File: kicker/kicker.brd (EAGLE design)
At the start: 59.7 x 56.3 mm, 27 parts, among them T1 NPN_BC817,215, T2 NPN_BC817,215, T3 NPN_BC817,215, T4 NPN_BC817,215, X1 JST-XH-06-PIN-LONG-PAD

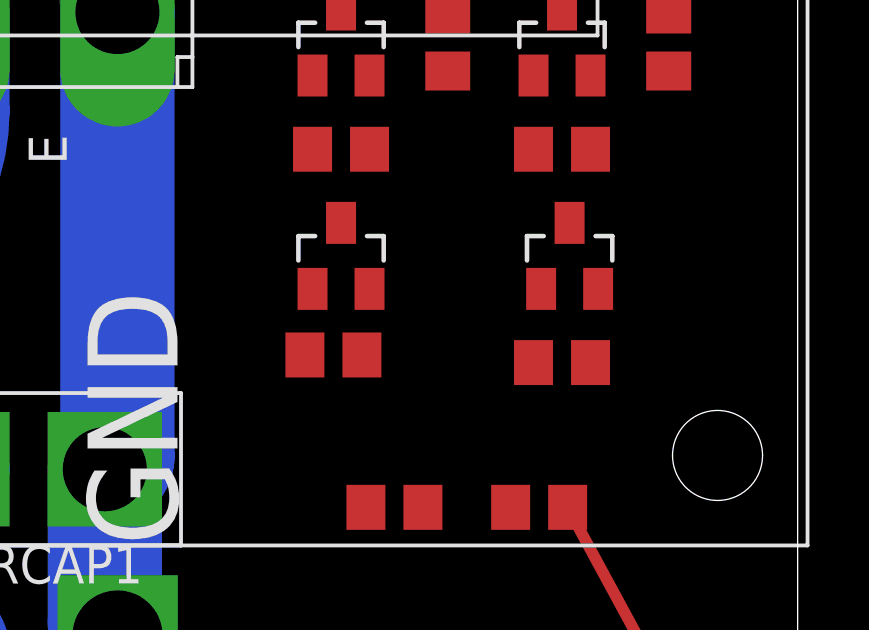
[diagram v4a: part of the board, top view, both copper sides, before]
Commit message: Adding optocoupler on the kick line
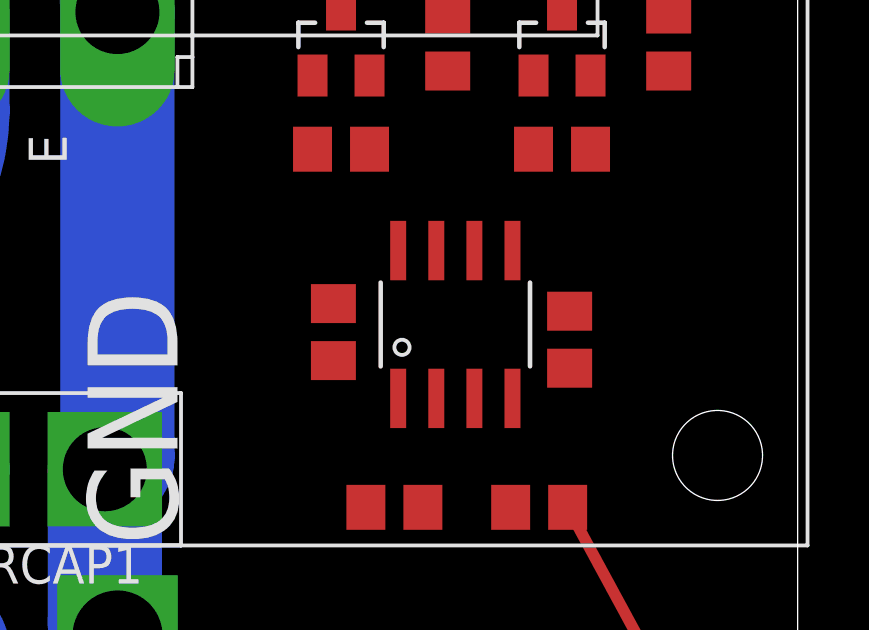
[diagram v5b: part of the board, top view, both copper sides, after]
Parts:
- removed R1, R4: 3K, rhoban:R0805
- removed T2, T4: NPN_BC817,215, rhoban:SOT-23
- added R7, R8: 3K, rhoban:R0805
- added U$4: ACPL-227-500E, rhoban:SO8
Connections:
- removed net N$1: R2.1, T1.1, T2.3
- removed net N$3: R32.1, T3.1, T4.3
- removed net N$5: R1.1, T2.1
- removed net N$6: R4.1, T4.1
- new net KICK_TR1: R2.1, T1.1
- new net KICK_TR2: R32.1, T3.1
- new net N$10: R8.1, U$4.3
- new net N$9: R7.1, U$4.1
- net GND: now also U$4.2, U$4.4; no longer T2.2, T4.2
- net KICK1: now also R7.2; no longer R1.2
- net KICK2: now also R8.2; no longer R4.2
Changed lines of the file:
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@@
 <element name="U$2" library="SparkFun-Hardware" package="STAND-OFF" value="" x="13.97" y="46.99"/>
 <element name="U$3" library="SparkFun-Hardware" package="STAND-OFF" value="" x="31.496" y="46.99"/>
-<element name="T2" library="rhoban" package="SOT-23" value="NPN_BC817,215" x="44.45" y="17.272">
-<attribute name="FARNELL" value="1081223" x="44.45" y="17.272" size="1.778" layer="27" display="off"/>
-</element>
-<element name="R1" library="rhoban" package="R0805" value="3K" x="44.196" y="13.97">
-<attribute name="FARNELL" value="2446965" x="44.196" y="13.97" size="1.778" layer="27" display="off"/>
-</element>
-<element name="T4" library="rhoban" package="SOT-23" value="NPN_BC817,215" x="52.07" y="17.272">
-<attribute name="FARNELL" value="1081223" x="52.07" y="17.272" size="1.778" layer="27" display="off"/>
-</element>
-<element name="R4" library="rhoban" package="R0805" value="3K" x="51.816" y="13.716">
-<attribute name="FARNELL" value="2446965" x="51.816" y="13.716" size="1.778" layer="27" display="off"/>
-</element>
 <element name="R5" library="rhoban" package="R0805" value="1K" x="44.45" y="28.702" rot="R270">
 <attribute name="FARNELL" value="2446965" x="44.45" y="28.702" size="1.778" layer="27" rot="R270" display="off"/>
@@
 <attribute name="FARNELL" value="2446965" x="51.816" y="28.702" size="1.778" layer="27" rot="R270" display="off"/>
 </element>
+<element name="U$4" library="rhoban" package="SO8" value="ACPL-227-500E" x="48.26" y="14.986" rot="R90">
+<attribute name="FARNELL" value="1634749RL" x="48.26" y="14.986" size="1.778" layer="27" rot="R90" display="off"/>
+</element>
+<element name="R7" library="rhoban" package="R0805" value="3K" x="44.196" y="14.732" rot="R90">
+<attribute name="FARNELL" value="2446965" x="44.196" y="14.732" size="1.778" layer="27" rot="R90" display="off"/>
+</element>
+<element name="R8" library="rhoban" package="R0805" value="3K" x="52.07" y="14.478" rot="R90">
+<attribute name="FARNELL" value="2446965" x="52.07" y="14.478" size="1.778" layer="27" rot="R90" display="off"/>
+</element>
 </elements>
 <signals>
 <signal name="KICK2">
 <contactref element="X1" pad="5"/>
-<contactref element="R4" pad="2"/>
-<wire x1="53.594" y1="1.27" x2="52.766" y2="13.716" width="0" layer="19" extent="1-1"/>
+<contactref element="R8" pad="2"/>
+<wire x1="52.07" y1="15.428" x2="53.594" y2="1.27" width="0" layer="19" extent="1-1"/>
 </signal>
 <signal name="GND" class="2">
@@
 <wire x1="25.654" y1="32.766" x2="29.63" y2="32.766" width="3.81" layer="16"/>
 <wire x1="29.63" y1="32.766" x2="36.996" y2="25.4" width="3.81" layer="16" curve="-90"/>
-<contactref element="T2" pad="2"/>
-<contactref element="T4" pad="2"/>
-<wire x1="53.02" y1="16.172" x2="52.766" y2="23.284" width="0" layer="19" extent="1-1"/>
+<contactref element="U$4" pad="2"/>
+<contactref element="U$4" pad="4"/>
 <wire x1="45.4" y1="23.284" x2="52.766" y2="23.284" width="0" layer="19" extent="1-1"/>
-<wire x1="45.4" y1="16.172" x2="45.4" y2="23.284" width="0" layer="19" extent="1-1"/>
-<wire x1="50.104" y1="8.89" x2="53.02" y2="16.172" width="0" layer="19" extent="1-1"/>
 <wire x1="36.996" y1="25.4" x2="45.4" y2="23.284" width="0" layer="19" extent="1-1"/>
 <wire x1="43.434" y1="1.27" x2="37" y2="0.17" width="0" layer="19" extent="16-16"/>
+<wire x1="50.104" y1="8.89" x2="43.434" y2="1.27" width="0" layer="19" extent="1-1"/>
 <wire x1="8.72" y1="14.92" x2="19.47" y2="25.4" width="0" layer="19" extent="1-1"/>
 <wire x1="11" y1="4.62" x2="8.72" y2="14.92" width="0" layer="19" extent="1-1"/>
+<wire x1="47.625" y1="12.5222" x2="11" y2="4.62" width="0" layer="19" extent="1-1"/>
+<wire x1="50.165" y1="12.5222" x2="47.625" y2="12.5222" width="0" layer="19" extent="1-1"/>
 </signal>
 <signal name="N$4">
@@
 <signal name="KICK1">
 <contactref element="X1" pad="4"/>
-<contactref element="R1" pad="2"/>
-<wire x1="51.054" y1="1.27" x2="45.146" y2="13.97" width="0" layer="19" extent="1-1"/>
+<contactref element="R7" pad="2"/>
+<wire x1="44.196" y1="15.682" x2="51.054" y2="1.27" width="0" layer="19" extent="1-1"/>
 </signal>
 <signal name="CAP">
@@
 <wire x1="6.52" y1="13.97" x2="3.81" y2="13.97" width="0.381" layer="1"/>
 </signal>
-<signal name="N$1">
+<signal name="KICK_TR1">
 <contactref element="R2" pad="1"/>
-<contactref element="T2" pad="3"/>
 <contactref element="T1" pad="1"/>
 <wire x1="43.5" y1="20.828" x2="43.5" y2="23.284" width="0" layer="19" extent="1-1"/>
-<wire x1="44.45" y1="18.372" x2="43.5" y2="20.828" width="0" layer="19" extent="1-1"/>
 </signal>
-<signal name="N$5">
-<contactref element="T2" pad="1"/>
-<contactref element="R1" pad="1"/>
-<wire x1="43.246" y1="13.97" x2="43.5" y2="16.172" width="0" layer="19" extent="1-1"/>
-</signal>
-<signal name="N$6">
-<contactref element="T4" pad="1"/>
-<contactref element="R4" pad="1"/>
-<wire x1="50.866" y1="13.716" x2="51.12" y2="16.172" width="0" layer="19" extent="1-1"/>
-</signal>
-<signal name="N$3">
-<contactref element="T4" pad="3"/>
+<signal name="KICK_TR2">
 <contactref element="R32" pad="1"/>
 <contactref element="T3" pad="1"/>
 <wire x1="50.866" y1="20.828" x2="50.866" y2="23.284" width="0" layer="19" extent="1-1"/>
-<wire x1="52.07" y1="18.372" x2="50.866" y2="20.828" width="0" layer="19" extent="1-1"/>
 </signal>
 <signal name="N$7">
@@
 <wire x1="8.47" y1="25.4" x2="51.816" y2="29.652" width="0" layer="19" extent="1-1"/>
 </signal>
+<signal name="N$9">
+<contactref element="U$4" pad="1"/>
+<contactref element="R7" pad="1"/>
+<wire x1="46.355" y1="12.5222" x2="44.196" y2="13.782" width="0" layer="19" extent="1-1"/>
+</signal>
+<signal name="N$10">
+<contactref element="U$4" pad="3"/>
+<contactref element="R8" pad="1"/>
+<wire x1="48.895" y1="12.5222" x2="52.07" y2="13.528" width="0" layer="19" extent="1-1"/>
+</signal>
 </signals>

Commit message: Fix optocoupler
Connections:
- net GND: now also U$4.5, U$4.7
- net KICK_TR1: now also U$4.8
- net KICK_TR2: now also U$4.6
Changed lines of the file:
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@@
 <contactref element="U$4" pad="2"/>
 <contactref element="U$4" pad="4"/>
-<wire x1="45.4" y1="23.284" x2="52.766" y2="23.284" width="0" layer="19" extent="1-1"/>
+<contactref element="U$4" pad="7"/>
+<contactref element="U$4" pad="5"/>
+<wire x1="50.165" y1="17.4498" x2="52.766" y2="23.284" width="0" layer="19" extent="1-1"/>
+<wire x1="47.625" y1="17.4498" x2="50.165" y2="17.4498" width="0" layer="19" extent="1-1"/>
+<wire x1="50.165" y1="12.5222" x2="50.165" y2="17.4498" width="0" layer="19" extent="1-1"/>
+<wire x1="47.625" y1="12.5222" x2="50.165" y2="12.5222" width="0" layer="19" extent="1-1"/>
+<wire x1="50.104" y1="8.89" x2="50.165" y2="12.5222" width="0" layer="19" extent="1-1"/>
+<wire x1="45.4" y1="23.284" x2="47.625" y2="17.4498" width="0" layer="19" extent="1-1"/>
 <wire x1="36.996" y1="25.4" x2="45.4" y2="23.284" width="0" layer="19" extent="1-1"/>
 <wire x1="43.434" y1="1.27" x2="37" y2="0.17" width="0" layer="19" extent="16-16"/>
-<wire x1="50.104" y1="8.89" x2="43.434" y2="1.27" width="0" layer="19" extent="1-1"/>
 <wire x1="8.72" y1="14.92" x2="19.47" y2="25.4" width="0" layer="19" extent="1-1"/>
 <wire x1="11" y1="4.62" x2="8.72" y2="14.92" width="0" layer="19" extent="1-1"/>
-<wire x1="47.625" y1="12.5222" x2="11" y2="4.62" width="0" layer="19" extent="1-1"/>
-<wire x1="50.165" y1="12.5222" x2="47.625" y2="12.5222" width="0" layer="19" extent="1-1"/>
 </signal>
 <signal name="N$4">
@@
 <contactref element="R2" pad="1"/>
 <contactref element="T1" pad="1"/>
+<contactref element="U$4" pad="8"/>
 <wire x1="43.5" y1="20.828" x2="43.5" y2="23.284" width="0" layer="19" extent="1-1"/>
+<wire x1="46.355" y1="17.4498" x2="43.5" y2="20.828" width="0" layer="19" extent="1-1"/>
 </signal>
 <signal name="KICK_TR2">
 <contactref element="R32" pad="1"/>
 <contactref element="T3" pad="1"/>
+<contactref element="U$4" pad="6"/>
 <wire x1="50.866" y1="20.828" x2="50.866" y2="23.284" width="0" layer="19" extent="1-1"/>
+<wire x1="48.895" y1="17.4498" x2="50.866" y2="20.828" width="0" layer="19" extent="1-1"/>
 </signal>
 <signal name="N$7">

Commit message: Arranging
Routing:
- net GND: track 50.5 -> 52.6 mm
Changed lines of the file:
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@@
 <wire x1="19.304" y1="25.4" x2="19.304" y2="26.162" width="3.81" layer="30"/>
 <wire x1="19.304" y1="26.162" x2="25.908" y2="32.766" width="3.81" layer="30" curve="-90"/>
-<wire x1="25.908" y1="32.766" x2="29.718" y2="32.766" width="3.81" layer="30"/>
-<wire x1="29.718" y1="32.766" x2="36.83" y2="25.654" width="3.81" layer="30" curve="-90"/>
+<wire x1="25.654" y1="32.766" x2="32.512" y2="32.766" width="3.81" layer="30"/>
+<wire x1="32.512" y1="32.766" x2="37.084" y2="28.194" width="3.81" layer="30" curve="-90"/>
+<wire x1="37.084" y1="28.194" x2="37.084" y2="25.654" width="3.81" layer="30"/>
 </plain>
 <attributes>
@@
 <param name="mtCopper" value="0.035mm 0.035mm 0.035mm 0.035mm 0.035mm 0.035mm 0.035mm 0.035mm 0.035mm 0.035mm 0.035mm 0.035mm 0.035mm 0.035mm 0.035mm 0.035mm"/>
 <param name="mtIsolate" value="1.5mm 0.15mm 0.2mm 0.15mm 0.2mm 0.15mm 0.2mm 0.15mm 0.2mm 0.15mm 0.2mm 0.15mm 0.2mm 0.15mm 0.2mm"/>
-<param name="mdWireWire" value="8mil"/>
+<param name="mdWireWire" value="10mil"/>
 <param name="mdWirePad" value="20mil"/>
 <param name="mdWireVia" value="20mil"/>
@@
 <wire x1="19.47" y1="25.4" x2="19.47" y2="26.582" width="3.81" layer="16"/>
 <wire x1="19.47" y1="26.582" x2="25.654" y2="32.766" width="3.81" layer="16" curve="-90"/>
-<wire x1="25.654" y1="32.766" x2="29.63" y2="32.766" width="3.81" layer="16"/>
-<wire x1="29.63" y1="32.766" x2="36.996" y2="25.4" width="3.81" layer="16" curve="-90"/>
+<wire x1="25.654" y1="32.766" x2="32.766" y2="32.766" width="3.81" layer="16"/>
 <contactref element="U$4" pad="2"/>
 <contactref element="U$4" pad="4"/>
@@
 <wire x1="8.72" y1="14.92" x2="19.47" y2="25.4" width="0" layer="19" extent="1-1"/>
 <wire x1="11" y1="4.62" x2="8.72" y2="14.92" width="0" layer="19" extent="1-1"/>
+<wire x1="32.766" y1="32.766" x2="37.084" y2="28.448" width="3.81" layer="16" curve="-90"/>
+<wire x1="37.084" y1="28.448" x2="37.084" y2="25.146" width="3.81" layer="16"/>
+<wire x1="37.084" y1="25.146" x2="36.996" y2="25.4" width="0" layer="19" extent="1-16"/>
 </signal>
 <signal name="N$4">
